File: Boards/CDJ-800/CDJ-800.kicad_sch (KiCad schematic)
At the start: 5 parts, among them J1 CN701, J2 CN53, U1 RP2040, U2 TXS0108EPW, U3 PCM5102A

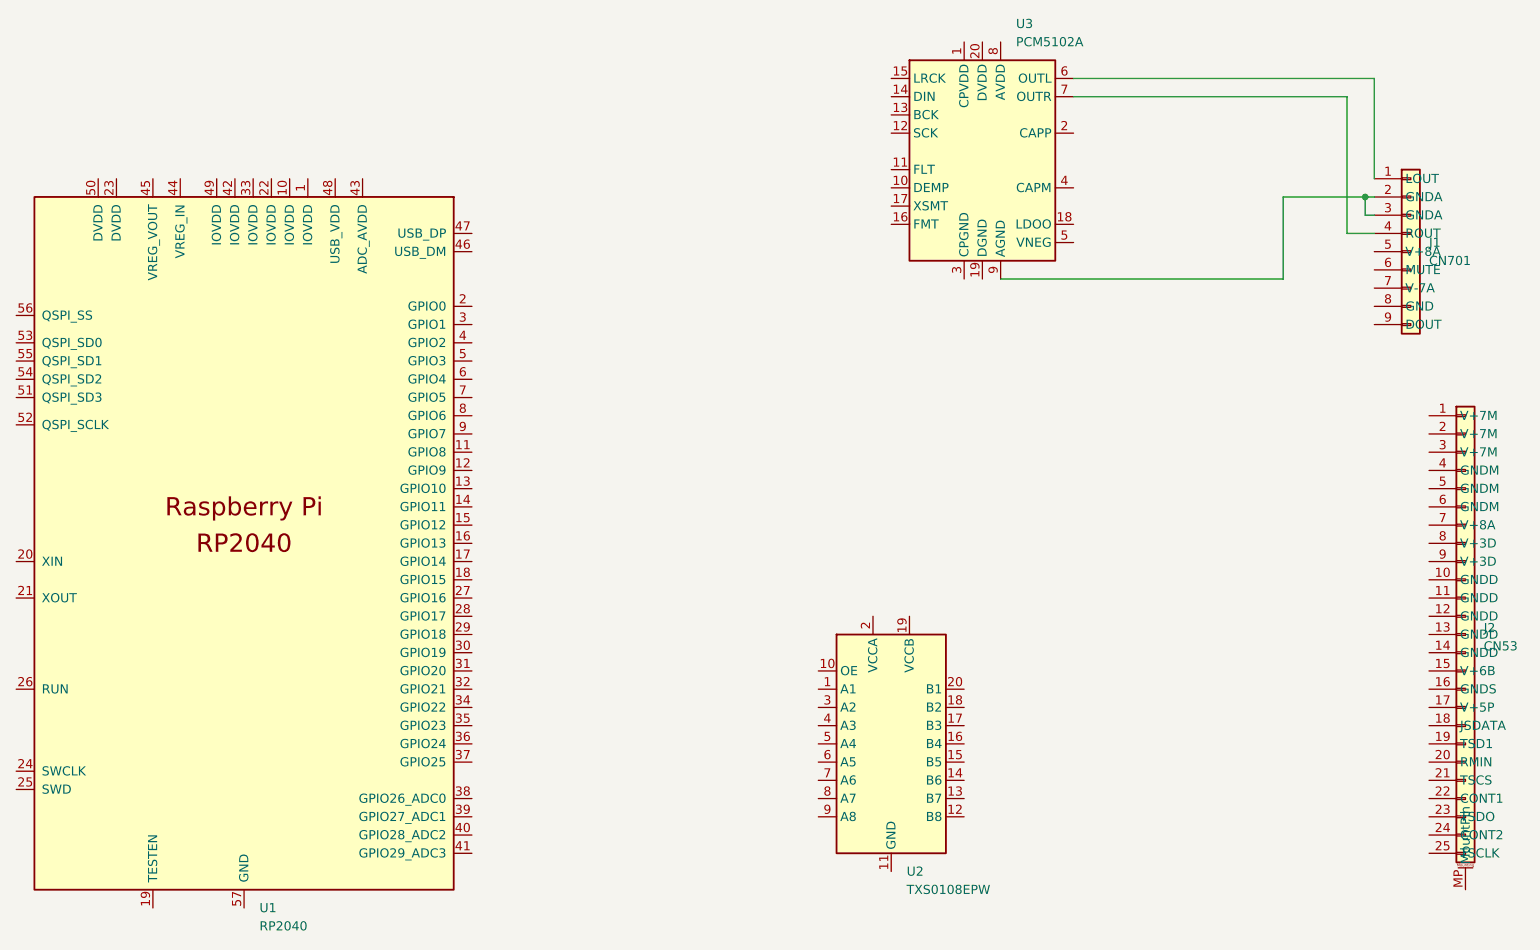
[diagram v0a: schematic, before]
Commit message: Reorganized folder structure for the 800 board
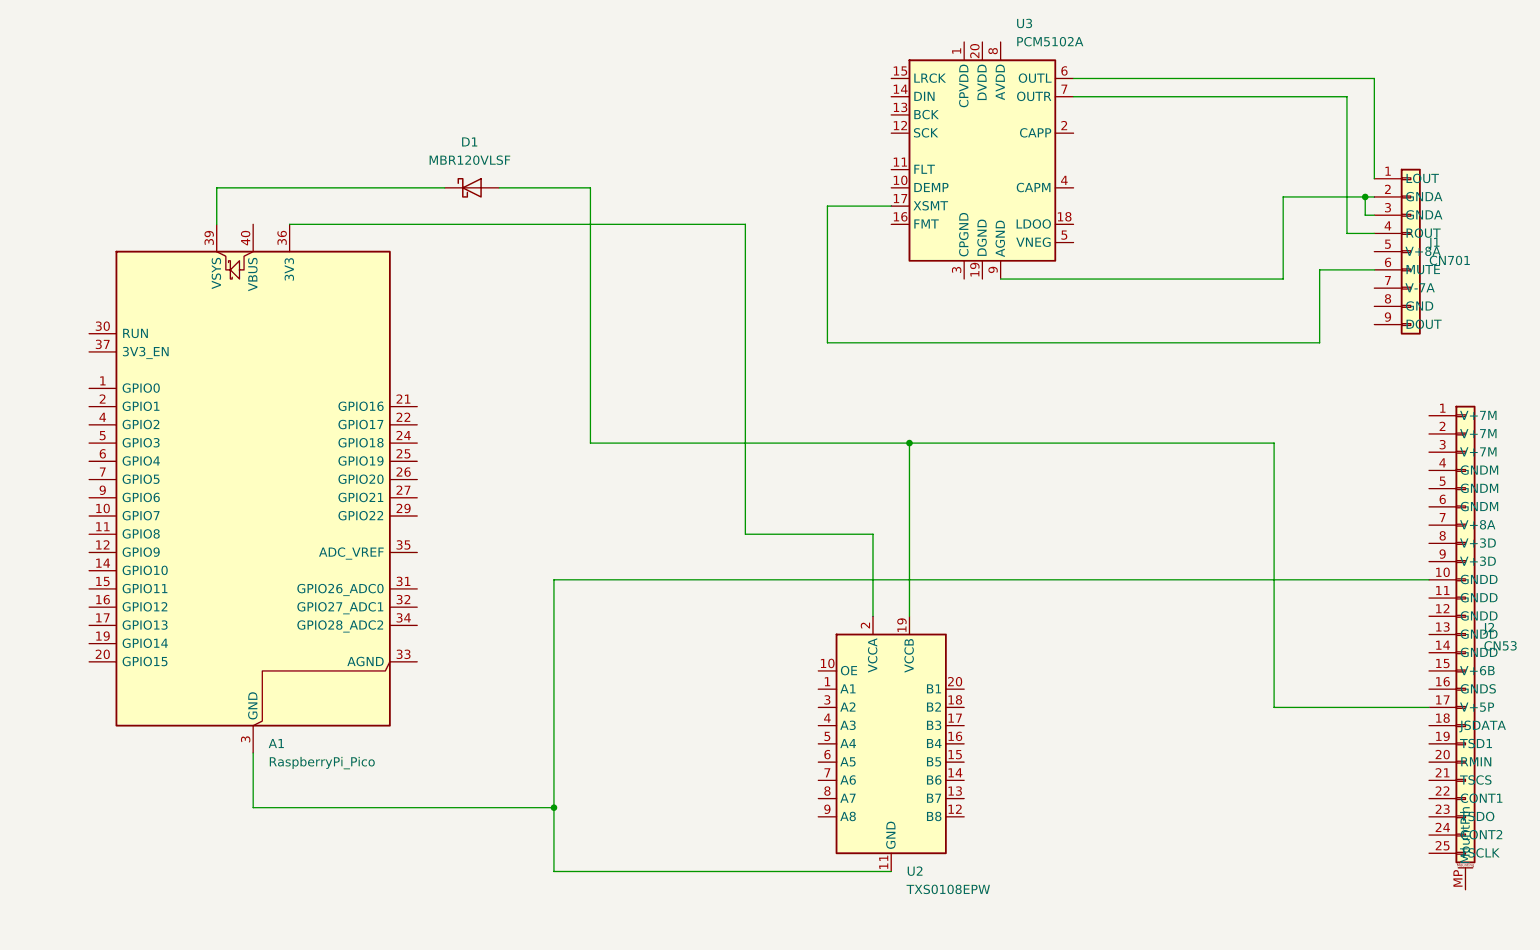
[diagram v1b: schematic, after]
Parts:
- removed U1: RP2040, RP2040_minimal:RP2040-QFN-56, symbol MCU_RaspberryPi_and_Boards:RP2040
- added A1: RaspberryPi_Pico, Module:RaspberryPi_Pico_Common_Unspecified, symbol MCU_Module:RaspberryPi_Pico
- added D1: MBR120VLSF, Diode_SMD:D_SOD-123F, symbol Diode:MBR1020VL
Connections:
- net at J2.10 (GNDD): now also U2.11 (GND), A1.13 (GND), A1.18 (GND), A1.23 (GND), A1.28 (GND), A1.3 (GND), A1.38 (GND), A1.8 (GND)
- net at J2.17 (V+5P): now also U2.19 (VCCB), D1.2 (A)
- net at U2.2 (VCCA): now also A1.36 (3V3)
- net at U3.17 (XSMT): now also J1.6 (MUTE)
- new net: A1.39 (VSYS), D1.1 (K)
